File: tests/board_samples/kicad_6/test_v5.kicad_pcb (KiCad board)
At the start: 2 copper layers, 22.9 x 16.5 mm, 20 parts

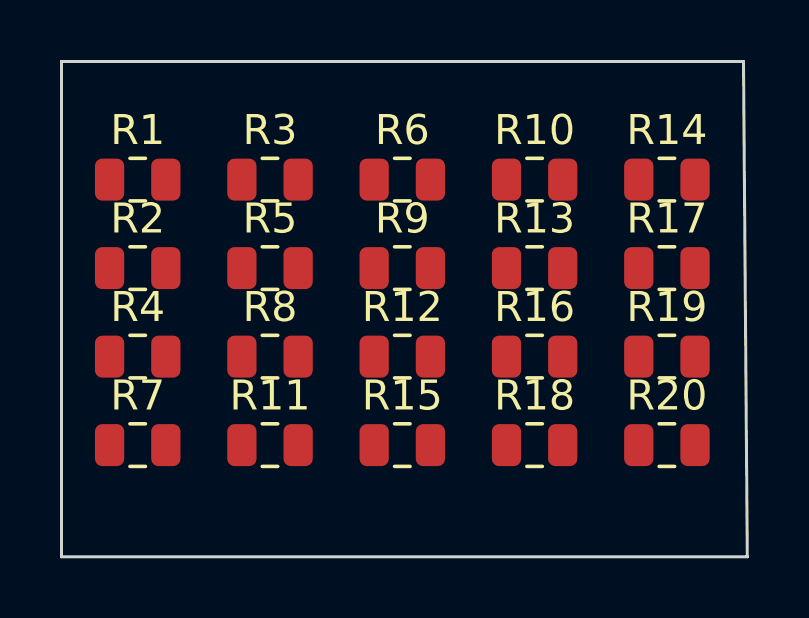
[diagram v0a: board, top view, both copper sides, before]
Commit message: [Tests] Adapted to the new behavior
- Removed bogus componentes in test_v5 PCBs
- Accounted for R3 in kibom-variant_3 PCB
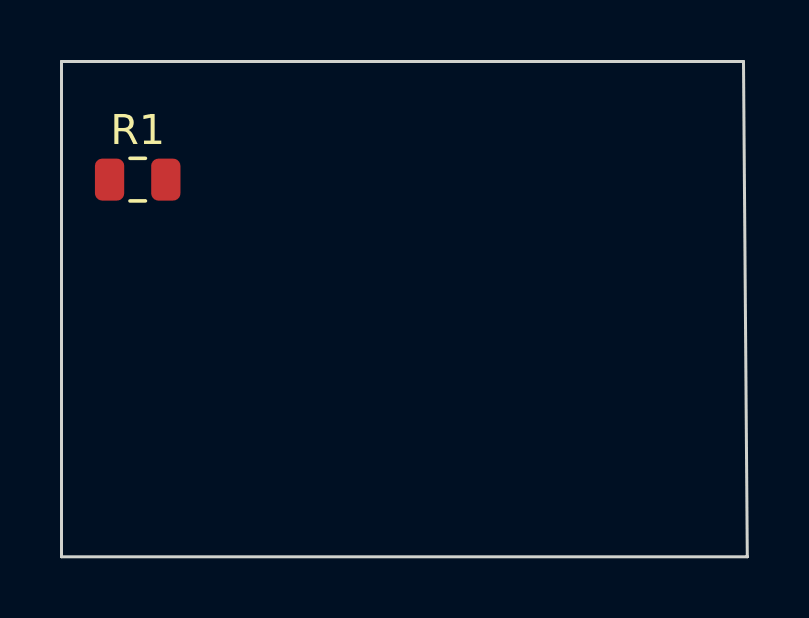
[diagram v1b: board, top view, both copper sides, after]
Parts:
- removed R10, R11, R12, R13, R14, R15, R16, R17, R18, R19, R20, R5, R6, R7, R8, R9: 10K, Resistor_SMD:R_0805_2012Metric
- removed R2: R_US, Resistor_SMD:R_0805_2012Metric
- removed R3, R4: 1m, Resistor_SMD:R_0805_2012Metric
